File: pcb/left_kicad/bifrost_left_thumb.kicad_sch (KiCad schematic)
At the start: 5 parts, among them SW41 UNASSIGNED_41, SW42 UNASSIGNED_42, SW43 UNASSIGNED_43

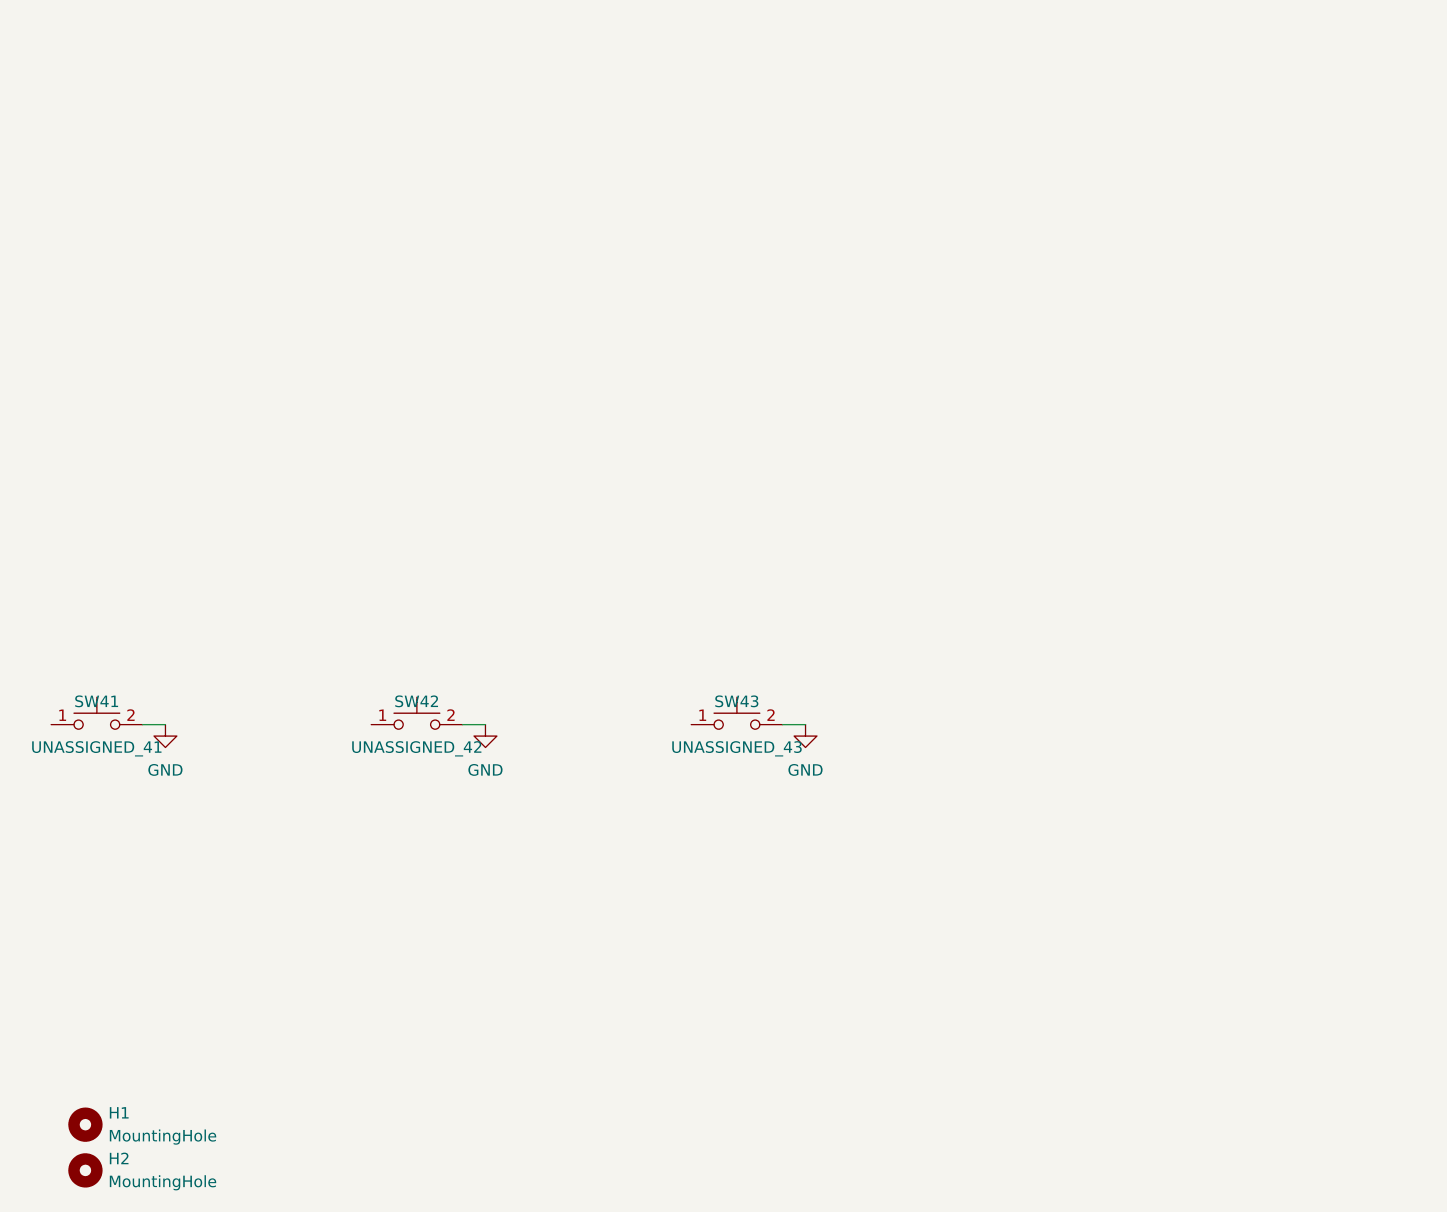
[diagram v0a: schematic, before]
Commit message: Update KiCad keyboard designs
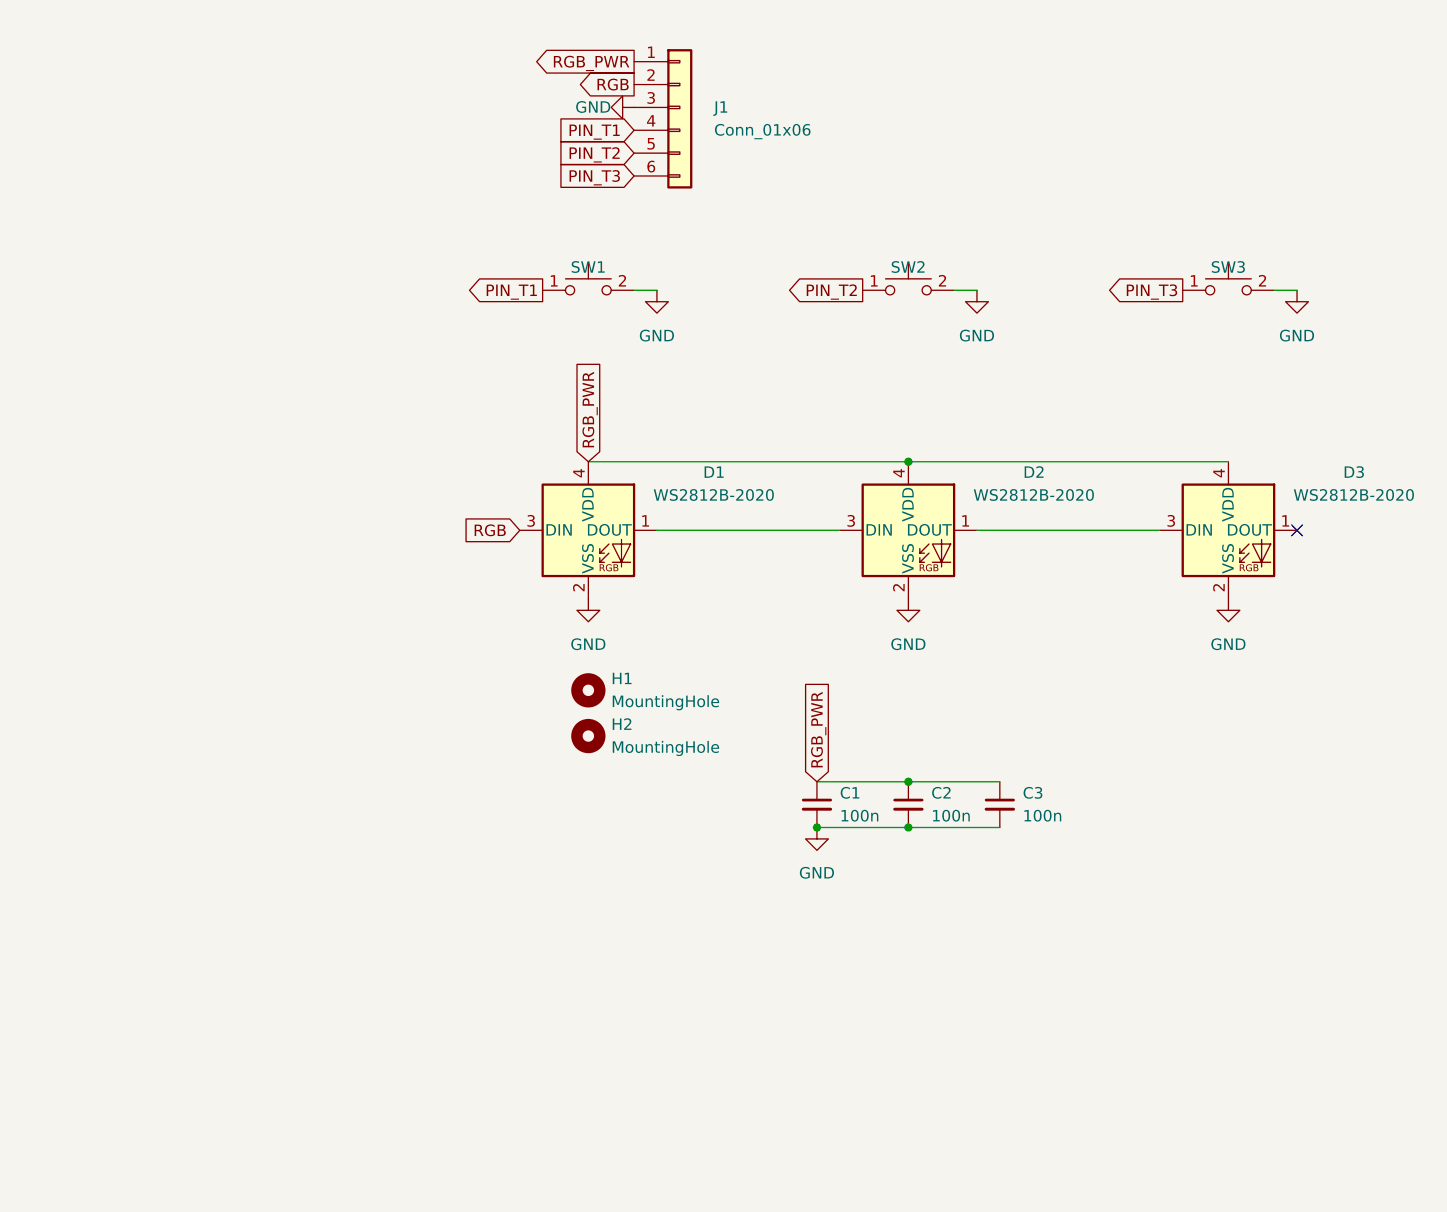
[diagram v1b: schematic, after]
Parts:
- added C1, C2, C3: 100n, Capacitor_SMD:C_0402_1005Metric, symbol Device:C_Small
- added D1, D2, D3: WS2812B-2020, LED_SMD:LED_WS2812B-2020_PLCC4_2.0x2.0mm, symbol LED:WS2812B-2020
- added J1: Conn_01x06, Connector_PinHeader_1.27mm:PinHeader_1x06_P1.27mm_Vertical, symbol Connector_Generic:Conn_01x06
- renumbered SW41 to SW1, SW42 to SW2, SW43 to SW3
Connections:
- net GND: now also C1.2, C2.2, C3.2, D1.2 (VSS), D2.2 (VSS), D3.2 (VSS), J1.3 (Pin_3)
- net PIN_T3: now reaches SW3.1
- net PIN_T3: now also J1.6 (Pin_6)
- net PIN_T2: now reaches SW2.1
- net PIN_T2: now also J1.5 (Pin_5)
- net PIN_T1: now reaches SW1.1
- net PIN_T1: now also J1.4 (Pin_4)
- new net: D2.1 (DOUT), D3.3 (DIN)
- new net: D1.1 (DOUT), D2.3 (DIN)
- new net RGB: D1.3 (DIN), J1.2 (Pin_2)
- new net RGB_PWR: C1.1, C2.1, C3.1, D1.4 (VDD), D2.4 (VDD), D3.4 (VDD), J1.1 (Pin_1)
- no-connect marks 0 -> 1
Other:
- moved on the sheet: H1, H2, SW1, SW2, SW3

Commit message: Use Old Norse Bifrǫst spelling
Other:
- title: Bifröst -> Bifrǫst
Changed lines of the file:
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@@
 	(paper "A4")
 	(title_block
-		(title "Bifröst")
+		(title "Bifrǫst")
 		(company "Hringbord")
 		(comment 1 "Generated by Smiðr KiCad export")

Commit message: Update PCB designs
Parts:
- SW1: value UNASSIGNED_41 -> 1U
- SW2: value UNASSIGNED_42 -> 1U
- SW3: value UNASSIGNED_43 -> 1U
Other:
- moved on the sheet: C1, C2, C3, D1, D2, D3, H1, H2, J1, SW1, SW2, SW3

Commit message: Update Bifrost case and PCB outputs
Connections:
- net GND: now also J1.2 (Pin_2); no longer J1.3 (Pin_3)
- net RGB: now also J1.3 (Pin_3); no longer J1.2 (Pin_2)
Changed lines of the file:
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@@
 	(global_label "RGB"
 		(shape output)
-		(at 76.2 78.74 180)
+		(at 76.2 81.28 180)
 		(fields_autoplaced yes)
 		(effects
@@
 		)
 		(property "Intersheetrefs" "${INTERSHEET_REFS}"
-			(at 69.4048 78.74 0)
+			(at 69.4048 81.28 0)
 			(hide yes)
 			(show_name no)
@@
 		(lib_name "GND_11")
 		(lib_id "power:GND")
-		(at 76.2 81.28 270)
+		(at 76.2 78.74 270)
 		(unit 1)
 		(body_style 1)
@@
 		(fields_autoplaced yes)
 		(property "Reference" "#PWR02"
-			(at 69.85 81.28 0)
+			(at 69.85 78.74 0)
 			(hide yes)
 			(show_name no)
@@
 		)
 		(property "Value" "GND"
-			(at 73.66 81.2799 90)
+			(at 73.66 78.7399 90)
 			(show_name no)
 			(do_not_autoplace no)
@@
 		)
 		(property "Footprint" ""
-			(at 76.2 81.28 0)
+			(at 76.2 78.74 0)
 			(hide yes)
 			(show_name no)
@@
 		)
 		(property "Datasheet" ""
-			(at 76.2 81.28 0)
+			(at 76.2 78.74 0)
 			(hide yes)
 			(show_name no)
@@
 		)
 		(property "Description" "Power symbol creates a global label with name \"GND\" , ground"
-			(at 76.2 81.28 0)
-			(hide yes)
-			(show_name no)
+			(at 76.2 78.74 0)
+			(hide yes)
+			(show_name no)

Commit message: Update PCB designs and production files
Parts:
- C1, C2, C3: JLCPCB Part # (none) -> C1525
- D1, D2, D3: JLCPCB Part # (none) -> C55109522
- J1: now left out of the parts list
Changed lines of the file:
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@@
+			)
+		)
+		(property "JLCPCB Part #" "C55109522"
+			(at 111.76 127 0)
+			(hide yes)
+			(show_name no)
+			(do_not_autoplace no)
+			(effects
+				(font
+					(size 1.27 1.27)
+				)
 			)
 		)
@@
 		(body_style 1)
 		(exclude_from_sim no)
-		(in_bom yes)
-		(on_board yes)
-		(in_pos_files yes)
+		(in_bom no)
+		(on_board yes)
+		(in_pos_files no)
 		(dnp no)
 		(fields_autoplaced yes)
@@
 			)
 		)
+		(property "JLCPCB Part #" "C1525 "
+			(at 121.92 154.94 0)
+			(hide yes)
+			(show_name no)
+			(do_not_autoplace no)
+			(effects
+				(font
+					(size 1.27 1.27)
+				)
+			)
+		)
 		(pin "1"
 		)
@@
 			)
 		)
+		(property "JLCPCB Part #" "C1525 "
+			(at 111.76 154.94 0)
+			(hide yes)
+			(show_name no)
+			(do_not_autoplace no)
+			(effects
+				(font
+					(size 1.27 1.27)
+				)
+			)
+		)
 		(pin "1"
 		)
@@
 			)
 		)
+		(property "JLCPCB Part #" "C1525 "
+			(at 101.6 154.94 0)
+			(hide yes)
+			(show_name no)
+			(do_not_autoplace no)
+			(effects
+				(font
+					(size 1.27 1.27)
+				)
+			)
+		)
 		(pin "1"
 		)
@@
 			)
 		)
+		(property "JLCPCB Part #" "C55109522"
+			(at 147.32 127 0)
+			(hide yes)
+			(show_name no)
+			(do_not_autoplace no)
+			(effects
+				(font
+					(size 1.27 1.27)
+				)
+			)
+		)
 		(pin "1"
 		)
@@
 			(at 76.2 127 0)
 			(hide yes)
+			(show_name no)
+			(do_not_autoplace no)
+			(effects
+				(font
+					(size 1.27 1.27)
+				)
+			)
+		)
+		(property "JLCPCB Part #" "C55109522"
+			(at 76.2 127 0)
+			(hide yes)

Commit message: Update PCB mounting hardware footprints
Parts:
- H1, H2: footprint Smidr:MountingHole_TH-1.6-M2 -> Smidr:SMD-1_BD4.4-D2.8; JLCPCB Part # C2928170 -> C2928179
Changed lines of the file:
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@@
 			)
 		)
-		(property "Footprint" "Smidr:MountingHole_TH-1.6-M2"
+		(property "Footprint" "Smidr:SMD-1_BD4.4-D2.8"
 			(at 76.2 152.4 0)
 			(hide yes)
@@
 			)
 		)
-		(property "JLCPCB Part #" "C2928170"
+		(property "JLCPCB Part #" "C2928179"
 			(at 76.2 152.4 0)
 			(hide yes)
@@
 			)
 		)
-		(property "Footprint" "Smidr:MountingHole_TH-1.6-M2"
+		(property "Footprint" "Smidr:SMD-1_BD4.4-D2.8"
 			(at 76.2 157.48 0)
 			(hide yes)
@@
 			)
 		)
-		(property "JLCPCB Part #" "C2928170"
+		(property "JLCPCB Part #" "C2928179"
 			(at 76.2 157.48 0)
 			(hide yes)
